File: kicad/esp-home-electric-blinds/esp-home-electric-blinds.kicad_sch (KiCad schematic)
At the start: 10 parts, among them J1 AC_IN, J2 Stepper_2_conn, J3 Stepper_2_conn, J4 Conn_01x05, U1 ESP32_mini, U2 TMC2208_Stepper_driver, U3 TMC2208_Stepper_driver

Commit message: assigned footprints
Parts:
- F1: footprint (none) -> components_johnymalina:car_fuse_holder
- J1: footprint (none) -> connectors_johnymalina:ScrewTerminal_01x02
- J2, J3: footprint (none) -> connectors_johnymalina:JST_smd_1x04_horizontal
- J4: footprint (none) -> connectors_johnymalina:JST_smd_1x05_horizontal
- U2, U3: footprint MODULE_TMC2208_SILENTSTEPSTICK -> components_johnymalina:TMC2208_Module
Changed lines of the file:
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@@
 			)
 		)
-		(property "Footprint" ""
+		(property "Footprint" "connectors_johnymalina:JST_smd_1x04_horizontal"
 			(at 360.68 100.33 0)
 			(effects
@@
 			)
 		)
-		(property "Footprint" ""
+		(property "Footprint" "components_johnymalina:car_fuse_holder"
 			(at 87.63 157.988 90)
 			(effects
@@
 			)
 		)
-		(property "Footprint" ""
+		(property "Footprint" "connectors_johnymalina:JST_smd_1x04_horizontal"
 			(at 360.68 172.72 0)
 			(effects
@@
 			)
 		)
-		(property "Footprint" ""
+		(property "Footprint" "connectors_johnymalina:ScrewTerminal_01x02"
 			(at 43.18 160.02 0)
 			(effects
@@
 			)
 		)
-		(property "Footprint" ""
+		(property "Footprint" "connectors_johnymalina:JST_smd_1x05_horizontal"
 			(at 210.82 232.41 0)
 			(effects
@@
 			)
 		)
-		(property "Footprint" "MODULE_TMC2208_SILENTSTEPSTICK"
+		(property "Footprint" "components_johnymalina:TMC2208_Module"
 			(at 330.2 100.33 0)
 			(effects
@@
 			)
 		)
-		(property "Footprint" "MODULE_TMC2208_SILENTSTEPSTICK"
+		(property "Footprint" "components_johnymalina:TMC2208_Module"
 			(at 330.2 172.72 0)
 			(effects

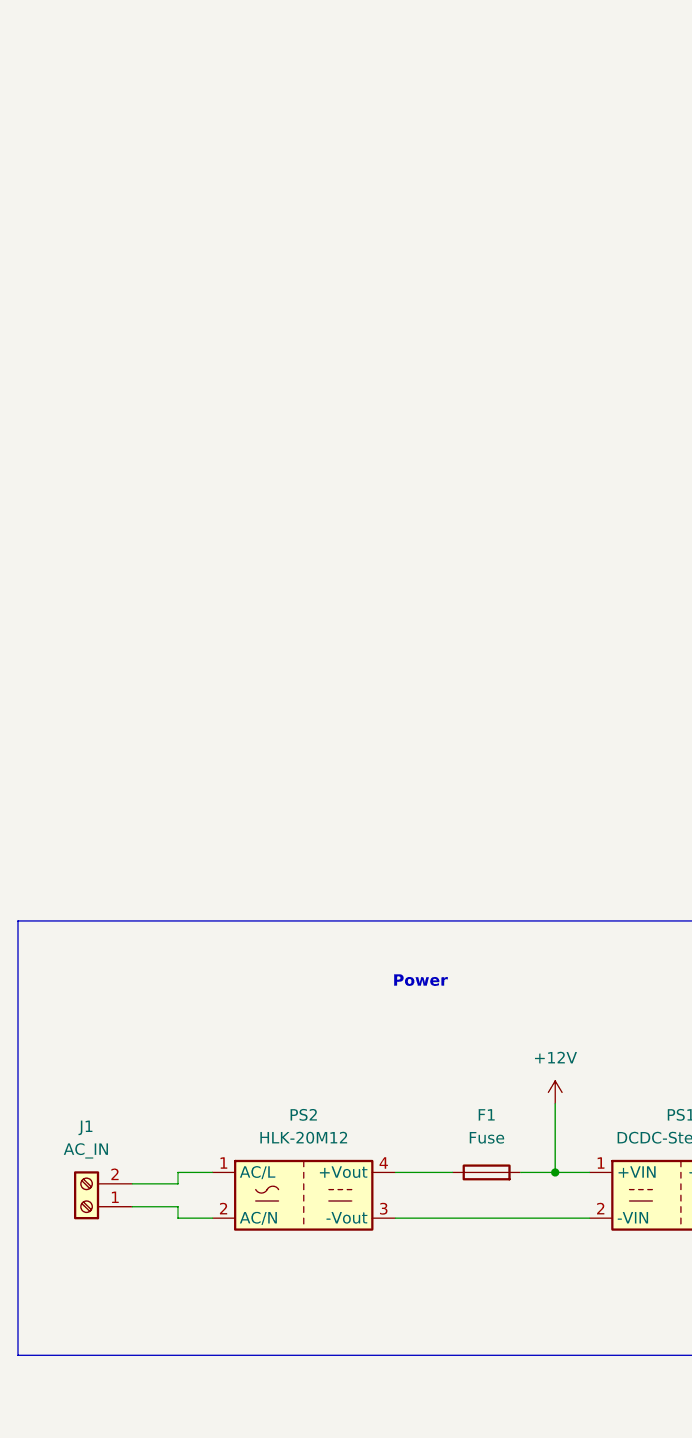
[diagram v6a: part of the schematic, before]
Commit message: mounting holes
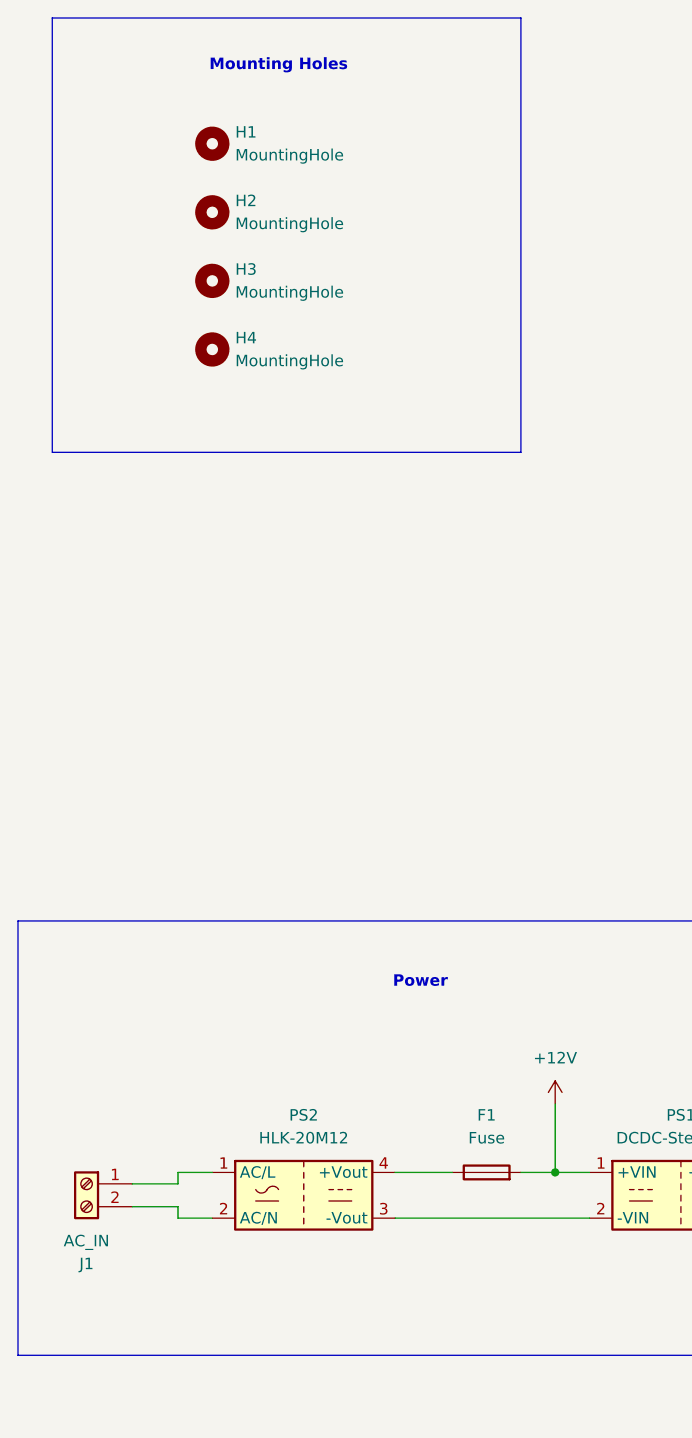
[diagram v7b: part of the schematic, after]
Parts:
- added H1, H2, H3, H4: MountingHole, MountingHole:MountingHole_2.7mm_M2.5, symbol Mechanical:MountingHole
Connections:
- net at J1.1 (Pin_1): now also PS2.1 (AC/L); no longer PS2.2 (AC/N)
- net at J1.2 (Pin_2): now also PS2.2 (AC/N); no longer PS2.1 (AC/L)
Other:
- note added: "Mounting Holes"
- moved on the sheet: J1
